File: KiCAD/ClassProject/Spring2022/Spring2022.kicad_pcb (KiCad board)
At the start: 2 copper layers, 211 x 39 mm, 64 parts, among them U1 FUB-MINI, U10 LM35-LP, U11 SHT40-AD1B-R3, U12 LIS2DE12TR, U2 74HC595, U3 74HC595, U4 74HC595, U5 74HC595, U6 74HC595, U7 74HC595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

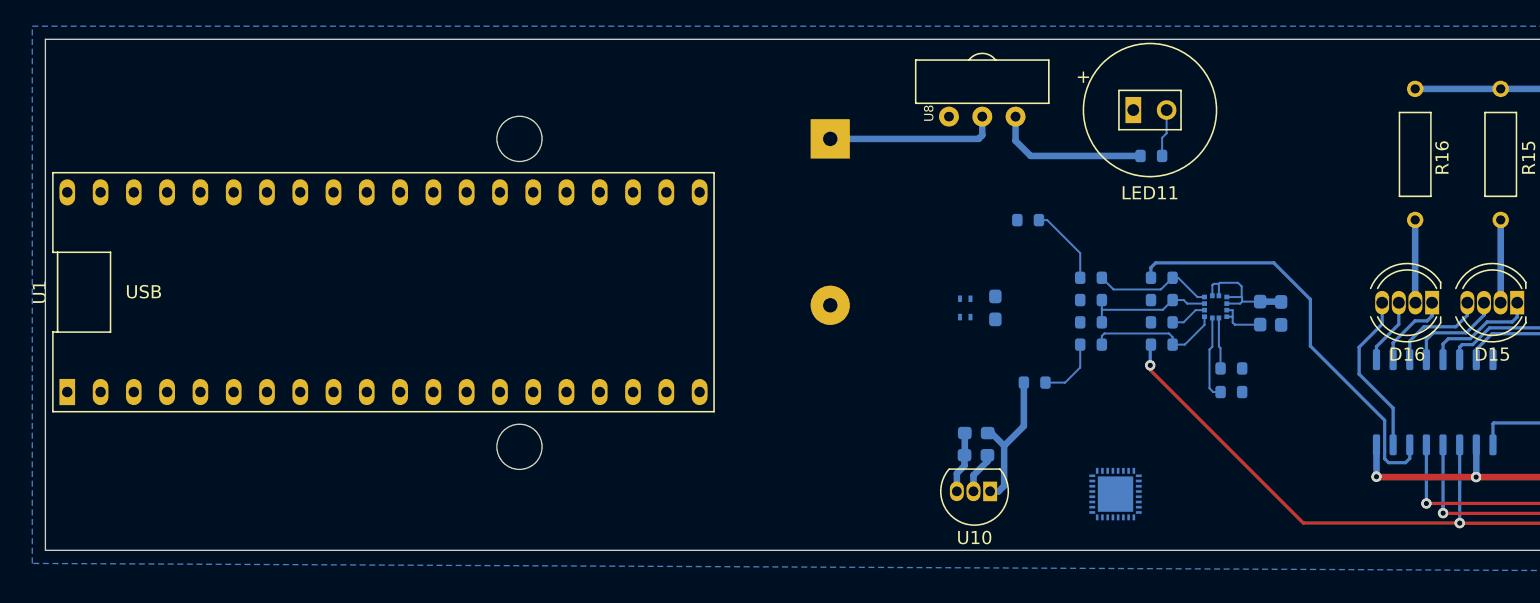
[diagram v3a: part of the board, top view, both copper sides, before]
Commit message: Added ESP32 but its going to come off before I am finished.
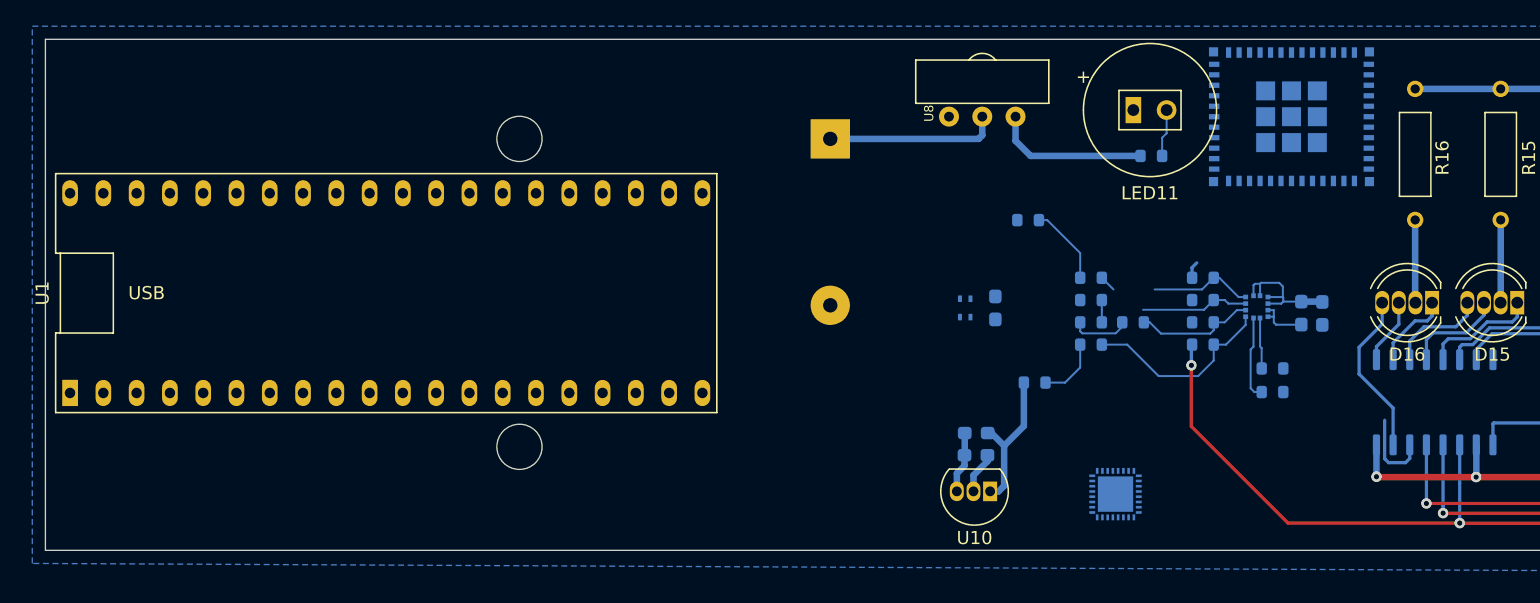
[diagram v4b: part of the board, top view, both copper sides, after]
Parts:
- added IC1: ESP32-C3-MINI-1-N4, 74_Patrick B:ESP32C3MINI1N4, B.Cu at (165.1, 25.9)
- added R30: PLP-000091, a_pontech:R_0603_1608Metric, B.Cu at (153.0, 41.6)
- moved R20 3.14 mm to (158.3, 43.3)
- moved R21 3.14 mm to (158.3, 38.2)
- moved R22 3.14 mm to (158.3, 39.9)
- moved R23 3.14 mm to (158.3, 41.6)
- moved R28 3.14 mm to (163.7, 46.9)
- moved R29 3.14 mm to (163.7, 45.1)
- moved C4 3.14 mm to (165.8, 40.9)
- moved C5 3.14 mm to (167.4, 40.9)
- moved U12 3.14 mm to (162.4, 40.4)
- moved U1 0.22 mm to (96.0, 39.4)
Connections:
- C2 pad 1: /Humi - Temp Sensor/Vtemp-Analog -> TEMPERATURE
- LED11 pad 1: /IR TX/RX/IR-TX -> IR-TX
- R23 pad 1: /Accelerometer/SPI-CS -> ~CS-ACC
- R24 pad 1: /Accelerometer/I2C-A0 -> (no net)
- R28 pad 2: /Accelerometer/INT1 -> ~INT1-ACC
- R29 pad 2: /Accelerometer/INT2 -> ~INT2-ACC
- U1 pad 1: Net-(U1-Pad1) -> (no net)
- U1 pad 10: Net-(U1-Pad10) -> ~INT1-ACC
- U1 pad 11: Net-(U1-Pad11) -> (no net)
- U1 pad 12: Net-(U1-Pad12) -> TEMPERATURE
- U1 pad 13: Net-(U1-Pad13) -> (no net)
- U1 pad 14: Net-(U1-Pad14) -> (no net)
- U1 pad 15: Net-(U1-Pad15) -> (no net)
- U1 pad 16: Net-(U1-Pad16) -> (no net)
- U1 pad 17: Net-(U1-Pad17) -> (no net)
- U1 pad 18: Net-(U1-Pad18) -> (no net)
- U1 pad 19: Net-(U1-Pad19) -> (no net)
- U1 pad 20: Net-(U1-Pad20) -> (no net)
- U1 pad 21: Net-(U1-Pad21) -> IR-TX
- U1 pad 24: Net-(U1-Pad24) -> (no net)
- U1 pad 25: Net-(U1-Pad25) -> DISPLAY-CLK
- U1 pad 26: Net-(U1-Pad26) -> ~LED-OE
- U1 pad 27: Net-(U1-Pad27) -> (no net)
- U1 pad 28: Net-(U1-Pad28) -> IR-RX
- U1 pad 31: Net-(U1-Pad31) -> (no net)
- U1 pad 32: Net-(U1-Pad32) -> (no net)
- U1 pad 33: Net-(U1-Pad33) -> (no net)
- U1 pad 34: Net-(U1-Pad34) -> (no net)
- U1 pad 35: Net-(U1-Pad35) -> (no net)
- U1 pad 36: Net-(U1-Pad36) -> (no net)
- U1 pad 37: Net-(U1-Pad37) -> (no net)
- U1 pad 4: Net-(U1-Pad4) -> (no net)
- U1 pad 5: Net-(U1-Pad5) -> (no net)
- U1 pad 6: Net-(U1-Pad6) -> (no net)
- U1 pad 8: Net-(U1-Pad8) -> ~INT2-ACC
- U1 pad 9: Net-(U1-Pad9) -> ~CS-ACC
- U10 pad 2: /Humi - Temp Sensor/Vtemp-Analog -> TEMPERATURE
- U12 pad 11: /Accelerometer/INT2 -> ~INT2-ACC
- U12 pad 12: /Accelerometer/INT1 -> ~INT1-ACC
- U2 pad 9: Net-(U2-Pad9) -> (no net)
- U8 pad 3: /IR TX/RX/IR-RX -> IR-RX
- U9 pad 1: Net-(U9-Pad1) -> (no net)
- U9 pad 10: Net-(U9-Pad10) -> (no net)
- U9 pad 11: Net-(U9-Pad11) -> (no net)
- U9 pad 12: Net-(U9-Pad12) -> (no net)
- U9 pad 13: Net-(U9-Pad13) -> (no net)
- U9 pad 14: Net-(U9-Pad14) -> (no net)
- U9 pad 15: Net-(U9-Pad15) -> (no net)
- U9 pad 16: Net-(U9-Pad16) -> (no net)
- U9 pad 17: Net-(U9-Pad17) -> (no net)
- U9 pad 18: Net-(U9-Pad18) -> (no net)
- U9 pad 19: Net-(U9-Pad19) -> (no net)
- U9 pad 2: Net-(U9-Pad2) -> (no net)
- U9 pad 20: Net-(U9-Pad20) -> (no net)
- U9 pad 21: Net-(U9-Pad21) -> (no net)
- U9 pad 22: Net-(U9-Pad22) -> (no net)
- U9 pad 23: Net-(U9-Pad23) -> (no net)
- U9 pad 24: Net-(U9-Pad24) -> (no net)
- U9 pad 25: Net-(U9-Pad25) -> (no net)
- U9 pad 26: Net-(U9-Pad26) -> (no net)
- U9 pad 27: Net-(U9-Pad27) -> (no net)
- U9 pad 28: Net-(U9-Pad28) -> (no net)
- U9 pad 29: Net-(U9-Pad29) -> (no net)
- U9 pad 3: Net-(U9-Pad3) -> (no net)
- U9 pad 30: Net-(U9-Pad30) -> (no net)
- U9 pad 31: Net-(U9-Pad31) -> (no net)
- U9 pad 32: Net-(U9-Pad32) -> (no net)
- U9 pad 4: Net-(U9-Pad4) -> (no net)
- U9 pad 5: Net-(U9-Pad5) -> (no net)
- U9 pad 6: Net-(U9-Pad6) -> (no net)
- U9 pad 7: Net-(U9-Pad7) -> (no net)
- U9 pad 8: Net-(U9-Pad8) -> (no net)
- U9 pad 9: Net-(U9-Pad9) -> (no net)
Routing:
- net MOSI: track 32.0 -> 7.43 mm
- net ~INT1-ACC: track 0.00 -> 6.42 mm
- net /Accelerometer/INT1: track 6.42 -> 0.00 mm
- net Net-(R23-Pad2): track 2.82 -> 9.21 mm
- net +3V3: track 15.4 -> 19.9 mm
- net Net-(R20-Pad2): track 10.5 -> 14.9 mm
- net ~INT2-ACC: track 0.00 -> 3.90 mm
- net /Accelerometer/INT2: track 3.90 -> 0.00 mm
- net TEMPERATURE: track 0.00 -> 3.20 mm
- net /Humi - Temp Sensor/Vtemp-Analog: track 3.20 -> 0.00 mm

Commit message: PCB Layout Complete.
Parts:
- removed IC1: ESP32-C3-MINI-1-N4, 74_Patrick B:ESP32C3MINI1N4
- removed U9: IS1871SF, 74_Kevin:Bluetooth_IC_IS1871SF-202-TRAY
- moved U10 36.4 mm to (163.7, 25.3), turned to 0 degrees
- moved C2 33.6 mm to (164.8, 28.0), turned to 0 degrees
- moved C1 31.3 mm to (164.8, 29.7), turned to 0 degrees
- moved R18 9.41 mm to (147.1, 43.0)
- moved R26 6.95 mm to (148.8, 50.2)
- moved R20 6.81 mm to (157.3, 50.0)
- moved R24 6.43 mm to (148.8, 46.2), turned to 180 degrees
- moved R27 6.43 mm to (148.8, 48.0)
- moved R28 6.43 mm to (162.6, 53.3)
- moved R29 6.43 mm to (162.6, 51.5)
- moved C5 6.43 mm to (166.4, 47.3)
- moved R22 6.43 mm to (157.3, 46.2)
- moved R23 6.43 mm to (157.3, 48.0)
- moved R30 6.43 mm to (152.0, 48.0)
- moved U11 6.43 mm to (139.2, 46.9)
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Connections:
- R24 pad 1: (no net) -> Net-(R22-Pad2)
- R24 pad 2: Net-(R22-Pad2) -> GND
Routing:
- net +4V: track 146.0 -> 412.3 mm
- net TEMPERATURE: track 3.20 -> 103.7 mm
- net ~LED-OE: track 120.1 -> 211.7 mm, vias 6 -> 7
- net DISPLAY-CLK: track 124.6 -> 216.0 mm, vias 6 -> 7
- net ~INT2-ACC: track 3.90 -> 86.5 mm, vias 0 -> 1
- net SCK: track 159.3 -> 235.8 mm
- net ~INT1-ACC: track 6.42 -> 82.6 mm, vias 0 -> 2
- net ~CS-ACC: track 0.00 -> 67.7 mm, vias 0 -> 1
- net I2C-SDA: track 6.08 -> 73.5 mm, vias 0 -> 1
- net MOSI: track 7.43 -> 72.4 mm, vias 0 -> 1
- net I2C-SCK: track 4.87 -> 61.5 mm, vias 0 -> 1
- net MISO: track 0.00 -> 51.8 mm, vias 0 -> 2
- net IR-RX: track 0.00 -> 43.7 mm
- net IR-TX: track 0.00 -> 37.6 mm
- net GND: track 124.8 -> 149.8 mm, vias 0 -> 1
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- added copper zone on F.Cu, net +3V3

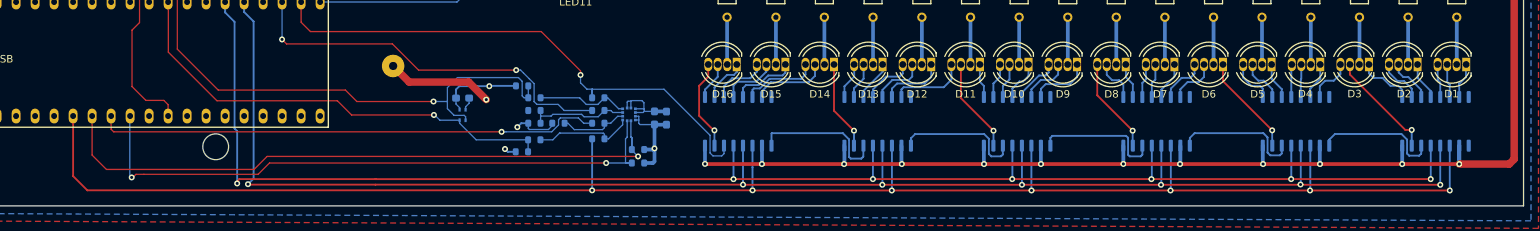
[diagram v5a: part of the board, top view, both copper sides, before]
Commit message: Added board name to silkscreen.
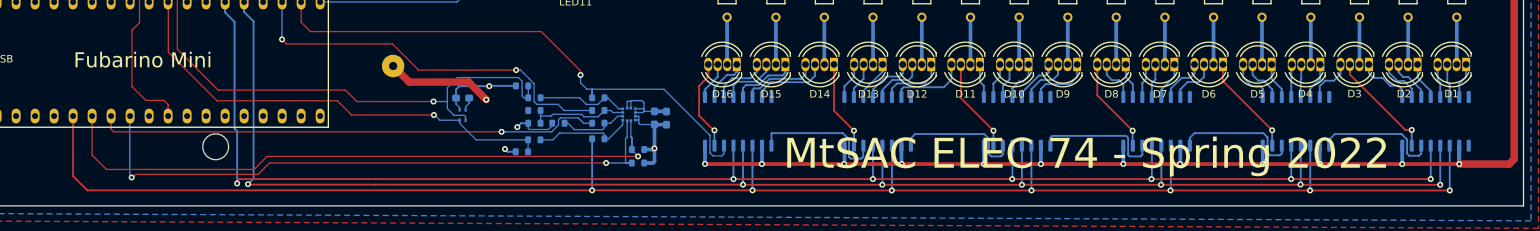
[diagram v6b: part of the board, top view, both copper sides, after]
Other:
- board text added: "Fubarino Mini"
- board text added: "MtSAC ELEC 74 - Spring 2022"

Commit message: Checking and gerber generation.
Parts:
- U12: value LIS2DE12TR -> LGA-12_STM
- moved C1 12.0 mm to (155.8, 37.7)
- moved BT1 12.0 mm to (120.9, 35.6)
- moved C2 12.0 mm to (155.8, 36.0)
- moved C3 12.0 mm to (130.2, 52.6)
- moved C4 12.0 mm to (155.8, 55.2)
- moved C5 12.0 mm to (157.4, 55.3)
- moved D1 12.0 mm to (264.3, 48.1)
- moved D10 12.0 mm to (205.8, 48.1)
- moved D11 12.0 mm to (199.3, 48.1)
- moved D12 12.0 mm to (192.8, 48.1)
- moved D13 12.0 mm to (186.3, 48.1)
- moved D14 12.0 mm to (179.8, 48.1)
- moved D15 12.0 mm to (173.3, 48.1)
- moved D16 12.0 mm to (166.8, 48.1)
- moved D2 12.0 mm to (257.8, 48.1)
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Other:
- net class Default: clearance 0.1524 -> 0.127; trace_width 0.1524 -> 0.127
- rule trace_clearance: 0.1524 -> 0.127
- rule trace_min: 0.1524 -> 0.127

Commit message: Upgraded to KiCAD 6.0
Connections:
- net ~CS-ACC renamed ~{CS-ACC}
- net ~INT1-ACC renamed ~{INT1-ACC}
- net ~INT2-ACC renamed ~{INT2-ACC}
- net ~LED-OE renamed ~{LED-OE}
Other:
- net class Default removed
